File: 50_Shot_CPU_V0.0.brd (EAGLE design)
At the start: 86 x 100 mm, 74 parts, among them IC1 PIC24FJ128GA010, J1 J12, J10 22-23-2021, J11 22-23-2061, J12 A311422_nd, J13 22-23-2021, J14 22-23-2021, J2 J2, J3 22-23-2021, J4 22-23-2021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

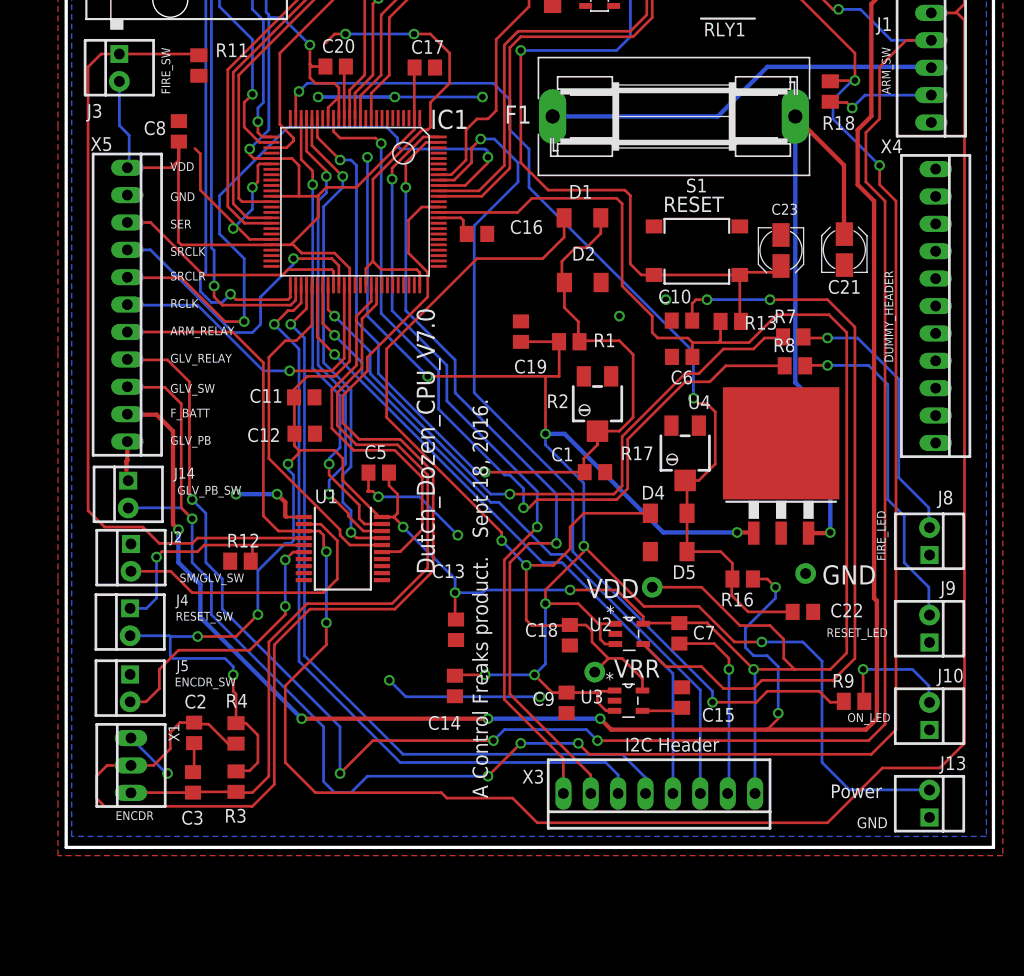
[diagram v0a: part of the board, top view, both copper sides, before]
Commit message: add relay board
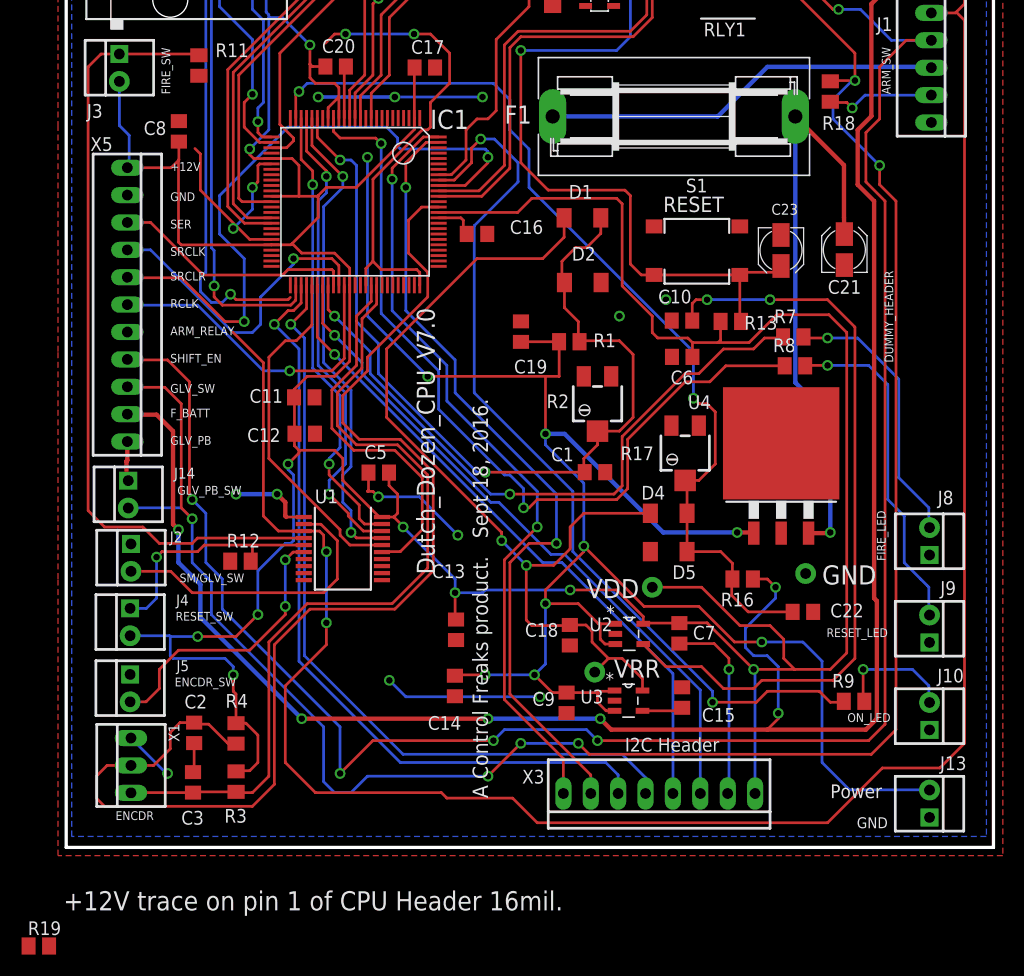
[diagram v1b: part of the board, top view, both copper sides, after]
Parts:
- removed X4: 22-23-2111, con-molex:22-23-2111
- added R19: 1k, rcl-2:M0805
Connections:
- removed net RF3: IC1.51, J11.1
- new net ###: J11.1
- new net SHIFT_EN: IC1.51, R19.1, X5.7
- net +12V: now also C8.1, J1.4, X5.1
- net ARM_RELAY: no longer X5.7
- net VCC: no longer J1.4
- net VDD: now also R19.2; no longer C8.1, X5.1
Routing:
- net RF3: track 55.3 -> 0.00 mm, vias 1 -> 0
- net ###: track 0.00 -> 54.2 mm, vias 0 -> 1
- net ARM_RELAY: track 212.2 -> 202.4 mm
- net VDD: track 416.8 -> 408.1 mm
- net +12V: track 171.7 -> 178.5 mm
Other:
- board text added: "+12V"
- board text added: "+12V trace on pin 1 of CPU Header 16mil."
- board text added: "SHIFT_EN"
- board text removed: "GLV_RELAY"
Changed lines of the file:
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@@
 <?xml version="1.0" encoding="utf-8"?>
 <!DOCTYPE eagle SYSTEM "eagle.dtd">
-<eagle version="7.6.0">
+<eagle version="7.7.0">
 <drawing>
 <settings>
@@
 <wire x1="0" y1="100" x2="0" y2="0" width="0.3048" layer="20"/>
 <text x="32.512" y="50.038" size="1.6764" layer="21" rot="R270">Dutch_Dozen_CPU_V7.0</text>
-<text x="9.652" y="62.738" size="0.8128" layer="21">VDD</text>
+<text x="9.652" y="62.738" size="0.8128" layer="21">+12V</text>
 <text x="9.652" y="59.944" size="0.8128" layer="21">GND</text>
 <text x="9.652" y="57.404" size="0.8128" layer="21">SER</text>
@@
 <text x="9.652" y="50.038" size="0.8128" layer="21">RCLK</text>
 <text x="9.652" y="47.498" size="0.8128" layer="21">ARM_RELAY</text>
-<text x="9.652" y="44.958" size="0.8128" layer="21">GLV_RELAY</text>
+<text x="9.652" y="44.958" size="0.8128" layer="21">SHIFT_EN</text>
 <text x="9.652" y="42.164" size="0.8128" layer="21">GLV_SW</text>
 <text x="9.652" y="39.878" size="0.8128" layer="21">F_BATT</text>
@@
 <text x="70.104" y="24.384" size="1.778" layer="21">GND</text>
 <text x="50.8" y="15.748" size="1.6764" layer="21">VRR</text>
+<text x="-0.254" y="-5.842" size="1.778" layer="21">+12V trace on pin 1 of CPU Header 16mil.</text>
 </plain>
 <attributes>
@@
 <attribute name="NAME" x="2.238" y="64.598" size="1.27" layer="25" ratio="10"/>
 </element>
-<element name="X4" library="con-molex" package="22-23-2111" value="22-23-2111" x="80.64" y="50.21" smashed="yes" rot="R270">
-<attribute name="MPN" value="22-23-2111" x="80.64" y="50.21" size="1.778" layer="27" rot="R270" display="off"/>
-<attribute name="OC_FARNELL" value="5388879" x="80.64" y="50.21" size="1.778" layer="27" rot="R270" display="off"/>
-<attribute name="MF" value="MOLEX" x="80.64" y="50.21" size="1.778" layer="27" rot="R270" display="off"/>
-<attribute name="OC_NEWARK" value="27C9916" x="80.64" y="50.21" size="1.778" layer="27" rot="R270" display="off"/>
-<attribute name="NAME" x="75.52" y="64.384" size="1.27" layer="25" ratio="10"/>
-</element>
 <element name="X1" library="Mine" package="22-23-2031" value="22-23-2031" x="6.008" y="7.6" smashed="yes" rot="R90">
 <attribute name="MPN" value="22-23-2031" x="6.008" y="7.6" size="1.778" layer="27" rot="R90" display="off"/>
@@
 <attribute name="NAME" x="70.104" y="66.548" size="1.27" layer="25"/>
 </element>
+<element name="R19" library="rcl-2" package="M0805" value="1k" x="-2.54" y="-9.144"/>
 </elements>
 <signals>
@@
 <wire x1="46.408" y1="14.358" x2="45.078" y2="14.358" width="0.254" layer="1"/>
 <wire x1="45.078" y1="14.358" x2="43.434" y2="16.002" width="0.254" layer="1"/>
+<contactref element="C8" pad="1"/>
+<contactref element="X5" pad="1"/>
+<wire x1="10.45" y1="65.46" x2="10.45" y2="63.754" width="0.254" layer="1"/>
+<wire x1="5.67" y1="63.04" x2="9.736" y2="63.04" width="0.254" layer="1"/>
+<wire x1="9.736" y1="63.04" x2="10.45" y2="63.754" width="0.254" layer="1"/>
+<contactref element="J1" pad="4"/>
+<wire x1="45.71" y1="46.9" x2="80.238" y2="72.314" width="0" layer="19" extent="1-1"/>
+<wire x1="10.45" y1="63.754" x2="27.94" y2="64.008" width="0" layer="19" extent="1-1"/>
 </signal>
 <signal name="GND">
@@
 <signal name="VCC">
 <contactref element="F1" pad="2"/>
-<contactref element="J1" pad="4"/>
-<wire x1="80.238" y1="72.314" x2="80.162" y2="72.39" width="0.4064" layer="16"/>
 <wire x1="80.162" y1="72.39" x2="65.024" y2="72.39" width="0.4064" layer="16"/>
 <wire x1="65.024" y1="72.39" x2="60.424" y2="67.79" width="0.4064" layer="16"/>
@@
 <contactref element="R4" pad="2"/>
 <contactref element="C4" pad="1"/>
-<contactref element="C8" pad="1"/>
-<contactref element="X5" pad="1"/>
 <contactref element="X3" pad="8"/>
 <contactref element="C7" pad="1"/>
@@
 <wire x1="22.352" y1="43.688" x2="21.13" y2="42.466" width="0.254" layer="1"/>
 <wire x1="21.13" y1="42.466" x2="21.13" y2="41.742" width="0.254" layer="1"/>
-<wire x1="10.45" y1="65.46" x2="10.45" y2="63.754" width="0.254" layer="1"/>
 <wire x1="10.414" y1="56.134" x2="10.668" y2="55.88" width="0.254" layer="1"/>
 <wire x1="10.668" y1="55.88" x2="19.03" y2="55.88" width="0.254" layer="1"/>
@@
 <wire x1="4.93" y1="66.952" x2="5.842" y2="66.04" width="0.254" layer="16"/>
 <wire x1="5.842" y1="66.04" x2="5.842" y2="63.212" width="0.254" layer="16"/>
-<wire x1="5.842" y1="63.212" x2="5.67" y2="63.04" width="0.254" layer="16"/>
 <wire x1="21.59" y1="36.83" x2="21.59" y2="36.576" width="0.254" layer="1"/>
 <wire x1="21.59" y1="36.576" x2="20.574" y2="35.56" width="0.254" layer="1"/>
@@
 <wire x1="20.32" y1="28.194" x2="17.78" y2="25.654" width="0.254" layer="16"/>
 <wire x1="17.78" y1="25.654" x2="17.78" y2="21.59" width="0.254" layer="16"/>
-<wire x1="5.67" y1="63.04" x2="9.736" y2="63.04" width="0.254" layer="1"/>
-<wire x1="9.736" y1="63.04" x2="10.45" y2="63.754" width="0.254" layer="1"/>
-<wire x1="10.45" y1="65.46" x2="10.45" y2="63.79" width="0.254" layer="1"/>
 <wire x1="10.45" y1="63.79" x2="10.414" y2="63.754" width="0.254" layer="1"/>
 <wire x1="10.414" y1="63.754" x2="10.414" y2="56.134" width="0.254" layer="1"/>
@@
 <wire x1="66.548" y1="17.526" x2="67.564" y2="16.51" width="0.254" layer="1"/>
 <wire x1="34.31" y1="94.64" x2="34.086" y2="94.864" width="0.254" layer="1"/>
+<contactref element="R19" pad="2"/>
+<wire x1="10.414" y1="63.754" x2="5.842" y2="63.212" width="0" layer="19" extent="1-16"/>
+<wire x1="-1.59" y1="-9.144" x2="15.756" y2="7.052" width="0" layer="19" extent="1-1"/>
 </signal>
 <signal name="SM_LED">
@@
 <wire x1="13.716" y1="55.372" x2="13.716" y2="52.07" width="0.254" layer="16"/>
 </signal>
-<signal name="RF3">
-<contactref element="IC1" pad="51"/>
+<signal name="###">
 <contactref element="J11" pad="1"/>
-<wire x1="20.79" y1="52.14" x2="20.79" y2="51.016" width="0.254" layer="1"/>
 <wire x1="20.79" y1="51.016" x2="20.574" y2="50.8" width="0.254" layer="1"/>
 <via x="15.24" y="51.308" extent="1-16" drill="0.6"/>
@@
 <contactref element="R10" pad="2"/>
 <contactref element="J1" pad="2"/>
-<contactref element="X5" pad="7"/>
-<wire x1="5.67" y1="47.8" x2="15.446" y2="47.8" width="0.254" layer="1"/>
 <wire x1="15.446" y1="47.8" x2="18.288" y2="44.958" width="0.254" layer="1"/>
 <wire x1="20.951" y1="29.341" x2="22.035" y2="29.341" width="0.254" layer="1"/>
@@
 <wire x1="74.092" y1="69.774" x2="80.238" y2="69.774" width="0.254" layer="16"/>
 </signal>
+<signal name="SHIFT_EN">
+<contactref element="X5" pad="7"/>
+<contactref element="IC1" pad="51"/>
+<contactref element="R19" pad="1"/>
+<wire x1="5.67" y1="47.8" x2="20.79" y2="52.14" width="0" layer="19" extent="1-1"/>
+<wire x1="-3.49" y1="-9.144" x2="5.67" y2="47.8" width="0" layer="19" extent="1-1"/>
+</signal>
 </signals>

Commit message: add proper relay board
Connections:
- net ARM_RELAY: now also X5.7
- net GLV_RELAY: no longer X5.8
- net SHIFT_EN: now also X5.8; no longer X5.7
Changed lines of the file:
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@@
 </signal>
 <signal name="GLV_RELAY">
-<contactref element="X5" pad="8"/>
 <contactref element="RLY1" pad="6"/>
 <contactref element="R14" pad="1"/>
 <contactref element="D3" pad="C"/>
-<wire x1="5.67" y1="45.26" x2="5.718" y2="45.212" width="0.254" layer="1"/>
 <wire x1="5.718" y1="45.212" x2="9.398" y2="45.212" width="0.254" layer="1"/>
 <wire x1="9.398" y1="45.212" x2="11.43" y2="43.18" width="0.254" layer="1"/>
@@
 <wire x1="19.681" y1="29.341" x2="18.288" y2="30.734" width="0.254" layer="1"/>
 <wire x1="18.288" y1="30.734" x2="18.288" y2="44.958" width="0.254" layer="1"/>
+<contactref element="X5" pad="7"/>
+<wire x1="15.446" y1="47.8" x2="5.67" y2="47.8" width="0" layer="19" extent="1-1"/>
 </signal>
 <signal name="GALV_OUT">
@@
 </signal>
 <signal name="SHIFT_EN">
-<contactref element="X5" pad="7"/>
 <contactref element="IC1" pad="51"/>
 <contactref element="R19" pad="1"/>
-<wire x1="5.67" y1="47.8" x2="20.79" y2="52.14" width="0" layer="19" extent="1-1"/>
-<wire x1="-3.49" y1="-9.144" x2="5.67" y2="47.8" width="0" layer="19" extent="1-1"/>
+<contactref element="X5" pad="8"/>
+<wire x1="5.67" y1="45.26" x2="20.79" y2="52.14" width="0" layer="19" extent="1-1"/>
+<wire x1="-3.49" y1="-9.144" x2="5.67" y2="45.26" width="0" layer="19" extent="1-1"/>
 </signal>
 </signals>

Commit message: removed SM switch (RB2)
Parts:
- removed J2: J2, Mine:22-23-2021
- added JP1: SHERLOCK_4PIN_RGT, Mine:SHERLOCK_4PIN_RGT
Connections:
- removed net N$2: J2.1, U1.2
- removed net SM_SW: IC1.23, U1.19
- new net RB2: IC1.23, JP1.3
- net ###: now also J11.2, J11.3, J11.4
- net +12V: no longer X5.1
- net GND: no longer J2.2
- net RB12: now also JP1.1; no longer J11.4
- net RB13: now also JP1.4; no longer J11.3
- net RF2: now also JP1.2; no longer J11.2
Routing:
- net SM_SW: track 42.5 -> 0.00 mm, vias 2 -> 0
- net RB2: track 0.00 -> 40.9 mm, vias 0 -> 2
- net N$2: track 27.8 -> 0.00 mm
- net +12V: track 178.5 -> 174.5 mm
- net RB12: track 45.3 -> 42.7 mm
- net RF2: track 55.5 -> 53.6 mm
- net RB13: track 47.1 -> 46.1 mm

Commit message: converted SPI display header
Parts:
- removed X2: 22-23-2071, con-molex:22-23-2071
- added JP2: SHERLOCK_8PIN_RGT, Mine:SHERLOCK_8PIN-RGT
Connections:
- net RB12 renamed RB12_X+
- net RB13 renamed RB13_Y-
- net RB2 renamed RB2_Y+
- net RF2 renamed RF2_X-
- new net RG7_MISO: IC1.11, JP2.8
- net +12V: now also C4.1, JP2.1
- net GND: now also JP2.2; no longer X2.2
- net RG0_DC: now also JP2.3; no longer X2.3
- net RG1_RES: now also JP2.6; no longer X2.6
- net RG6_SCLK: now also JP2.4; no longer X2.4
- net RG8_MOSI: now also JP2.5; no longer X2.5
- net RG9_CS: now also JP2.7; no longer X2.7
- net VDD: no longer C4.1, X2.1
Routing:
- net RG1_RES: track 61.8 -> 59.9 mm
- net VDD: track 408.1 -> 407.4 mm
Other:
- board text added: "SPI Display Header"
- board text added: "Touch"

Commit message: converted rotary encoder header
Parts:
- removed X1: 22-23-2031, Mine:22-23-2031
- added JP3: SHERLOCK_3PIN_RGT, Mine:SHERLOCK_3PIN_RGT
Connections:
- net ENCDR_A: now also JP3.1; no longer X1.1
- net ENCDR_B: now also JP3.2; no longer X1.2
- net GND: now also JP3.3; no longer X1.3
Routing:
- net GND: track 133.4 -> 128.6 mm, vias 17 -> 16
- net ENCDR_B: track 112.5 -> 108.1 mm
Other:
- board text added: "Rotary Encoder"
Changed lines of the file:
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@@
 <text x="70.104" y="24.384" size="1.778" layer="21">GND</text>
 <text x="50.8" y="15.748" size="1.6764" layer="21">VRR</text>
-<text x="-0.254" y="-5.842" size="1.778" layer="21">+12V trace on pin 1 of CPU Header 16mil.</text>
+<text x="90.424" y="97.282" size="1.778" layer="21">+12V trace on pin 1 of CPU Header 16mil.</text>
 <text x="2.794" y="-16.002" size="1.016" layer="21">Touch</text>
 <text x="1.27" y="-28.194" size="1.016" layer="21">SPI Display Header</text>
+<text x="1.27" y="-41.91" size="1.016" layer="21">Rotary
+Encoder</text>
 </plain>
 <attributes>
@@
 <attribute name="NAME" x="2.238" y="64.598" size="1.27" layer="25" ratio="10"/>
 </element>
-<element name="X1" library="Mine" package="22-23-2031" value="22-23-2031" x="6.008" y="7.6" smashed="yes" rot="R90">
-<attribute name="MPN" value="22-23-2031" x="6.008" y="7.6" size="1.778" layer="27" rot="R90" display="off"/>
-<attribute name="OC_FARNELL" value="1462950" x="6.008" y="7.6" size="1.778" layer="27" rot="R90" display="off"/>
-<attribute name="MF" value="MOLEX" x="6.008" y="7.6" size="1.778" layer="27" rot="R90" display="off"/>
-<attribute name="OC_NEWARK" value="30C0862" x="6.008" y="7.6" size="1.778" layer="27" rot="R90" display="off"/>
-<attribute name="NAME" x="9.486" y="11.45" size="1.016" layer="25" ratio="10" rot="R270"/>
-</element>
 <element name="X3" library="con-molex" package="22-23-2081" value="22-23-2081" x="55" y="5" smashed="yes" rot="MR180">
 <attribute name="MPN" value="22-23-2081" x="55" y="5" size="1.778" layer="28" rot="MR180" display="off"/>
@@
 <element name="JP1" library="Mine" package="SHERLOCK_4PIN_RGT" value="SHERLOCK_4PIN_RGT" x="5.08" y="-20.574"/>
 <element name="JP2" library="Mine" package="SHERLOCK_8PIN-RGT" value="SHERLOCK_8PIN_RGT" x="8.89" y="-33.782"/>
+<element name="JP3" library="Mine" package="SHERLOCK_3PIN_RGT" value="SHERLOCK_3PIN_RGT" x="4.064" y="-46.99"/>
 </elements>
 <signals>
@@
 <contactref element="C2" pad="2"/>
 <contactref element="C3" pad="2"/>
-<contactref element="X1" pad="3"/>
 <contactref element="C10" pad="2"/>
 <contactref element="C13" pad="2"/>
@@
 <wire x1="11.762" y1="6.982" x2="11.866" y2="6.982" width="0.254" layer="1"/>
 <wire x1="11.866" y1="6.982" x2="11.866" y2="9.674" width="0.254" layer="1"/>
-<via x="9.398" y="6.858" extent="1-16" drill="0.6"/>
-<wire x1="6.008" y1="10.14" x2="9.29" y2="6.858" width="0.254" layer="16"/>
-<wire x1="9.29" y1="6.858" x2="9.398" y2="6.858" width="0.254" layer="16"/>
 <via x="15.748" y="32.766" extent="1-16" drill="0.6"/>
 <wire x1="22.035" y1="30.641" x2="20.413" y2="30.641" width="0.254" layer="1"/>
@@
 <via x="68.58" y="25.4" extent="1-16" drill="1" diameter="1.9304" shape="octagon"/>
 <contactref element="JP2" pad="2"/>
+<contactref element="JP3" pad="3"/>
 <wire x1="80.07" y1="84.23" x2="80.07" y2="92.34" width="0" layer="19" extent="1-1"/>
 <wire x1="73.024" y1="82.444" x2="80.07" y2="84.23" width="0" layer="19" extent="1-1"/>
@@
 <wire x1="26.192" y1="94.864" x2="30.886" y2="88.65" width="0" layer="19" extent="1-1"/>
 <wire x1="5.93" y1="16.042" x2="15.2098" y2="26.5444" width="0" layer="19" extent="1-1"/>
-<wire x1="6.008" y1="10.14" x2="5.93" y2="16.042" width="0" layer="19" extent="1-1"/>
-<wire x1="11.762" y1="6.982" x2="9.398" y2="6.858" width="0" layer="19" extent="1-1"/>
+<wire x1="11.866" y1="9.674" x2="5.93" y2="16.042" width="0" layer="19" extent="1-1"/>
 <wire x1="13.89" y1="-33.782" x2="11.762" y2="6.982" width="0" layer="19" extent="1-1"/>
+<wire x1="2.064" y1="-46.99" x2="13.89" y2="-33.782" width="0" layer="19" extent="1-1"/>
 </signal>
 <signal name="VCC">
@@
 <contactref element="IC1" pad="67"/>
 <contactref element="R3" pad="1"/>
-<contactref element="X1" pad="1"/>
 <contactref element="C3" pad="1"/>
 <wire x1="28.79" y1="52.14" x2="28.79" y2="50.38" width="0.254" layer="1"/>
@@
 <wire x1="33.528" y1="25.908" x2="30.226" y2="22.606" width="0.254" layer="1"/>
 <wire x1="22.352" y1="22.606" x2="18.796" y2="19.05" width="0.254" layer="1"/>
-<wire x1="6.008" y1="5.06" x2="6.03" y2="5.082" width="0.254" layer="1"/>
 <wire x1="6.03" y1="5.082" x2="11.762" y2="5.082" width="0.254" layer="1"/>
 <wire x1="11.762" y1="5.082" x2="11.832" y2="5.152" width="0.254" layer="1"/>
@@
 <wire x1="17.272" y1="5.08" x2="18.796" y2="6.604" width="0.254" layer="1"/>
 <wire x1="33.528" y1="34.544" x2="33.528" y2="25.908" width="0.254" layer="1"/>
+<contactref element="JP3" pad="1"/>
+<wire x1="6.03" y1="5.082" x2="6.064" y2="-46.99" width="0" layer="19" extent="1-1"/>
 </signal>
 <signal name="ENCDR_B">
 <contactref element="IC1" pad="87"/>
 <contactref element="C2" pad="1"/>
-<contactref element="X1" pad="2"/>
 <contactref element="R4" pad="1"/>
 <wire x1="34.54" y1="59.39" x2="32.974" y2="59.39" width="0.254" layer="1"/>
@@
 <wire x1="2.794" y1="4.572" x2="2.794" y2="6.604" width="0.254" layer="1"/>
 <wire x1="2.794" y1="6.604" x2="3.79" y2="7.6" width="0.254" layer="1"/>
-<wire x1="3.79" y1="7.6" x2="6.008" y2="7.6" width="0.254" layer="1"/>
 <wire x1="34.036" y1="34.798" x2="34.036" y2="25.654" width="0.254" layer="1"/>
 <wire x1="11.866" y1="11.574" x2="10.558" y2="11.574" width="0.254" layer="1"/>
@@
 <wire x1="9.652" y1="10.668" x2="9.652" y2="9.144" width="0.254" layer="1"/>
 <wire x1="9.652" y1="9.144" x2="8.108" y2="7.6" width="0.254" layer="1"/>
-<wire x1="8.108" y1="7.6" x2="6.008" y2="7.6" width="0.254" layer="1"/>
 <wire x1="11.866" y1="11.574" x2="12.01" y2="11.43" width="0.254" layer="1"/>
 <wire x1="12.01" y1="11.43" x2="13.208" y2="11.43" width="0.254" layer="1"/>
 <wire x1="13.208" y1="11.43" x2="15.016" y2="9.622" width="0.254" layer="1"/>
 <wire x1="15.016" y1="9.622" x2="15.748" y2="9.622" width="0.254" layer="1"/>
+<contactref element="JP3" pad="2"/>
+<wire x1="3.556" y1="3.81" x2="4.064" y2="-46.99" width="0" layer="19" extent="1-1"/>
+<wire x1="8.108" y1="7.6" x2="3.79" y2="7.6" width="0" layer="19" extent="1-1"/>
 </signal>
 <signal name="RCLK">
@@
 </board>
 </drawing>
+<compatibility>
+<note version="6.3" minversion="6.2.2" severity="warning">
+Since Version 6.2.2 text objects can contain more than one line,
+which will not be processed correctly with this version.
+</note>
+</compatibility>
 </eagle>
